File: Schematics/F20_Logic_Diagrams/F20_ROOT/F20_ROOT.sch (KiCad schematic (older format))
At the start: 0 parts

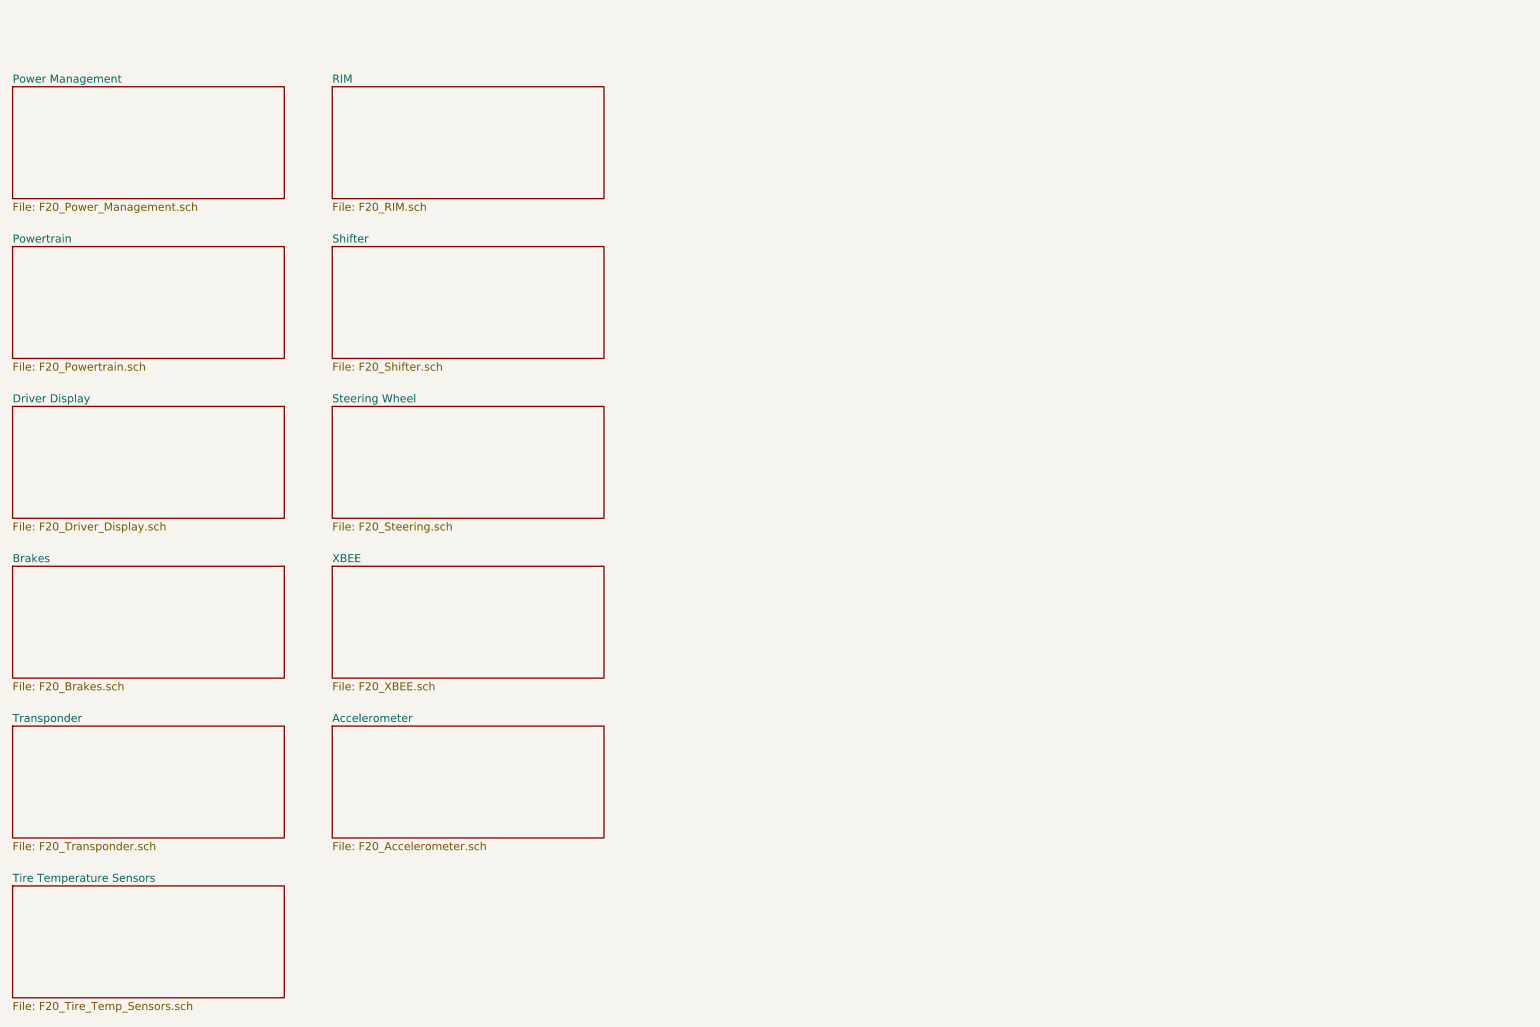
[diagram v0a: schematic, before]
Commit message: Added PDM Layout guide, updated Powertrain wiring, added a Master Connector Pinout guide, added TOC to LogicDiagrams pdf and rearranged them a bit.
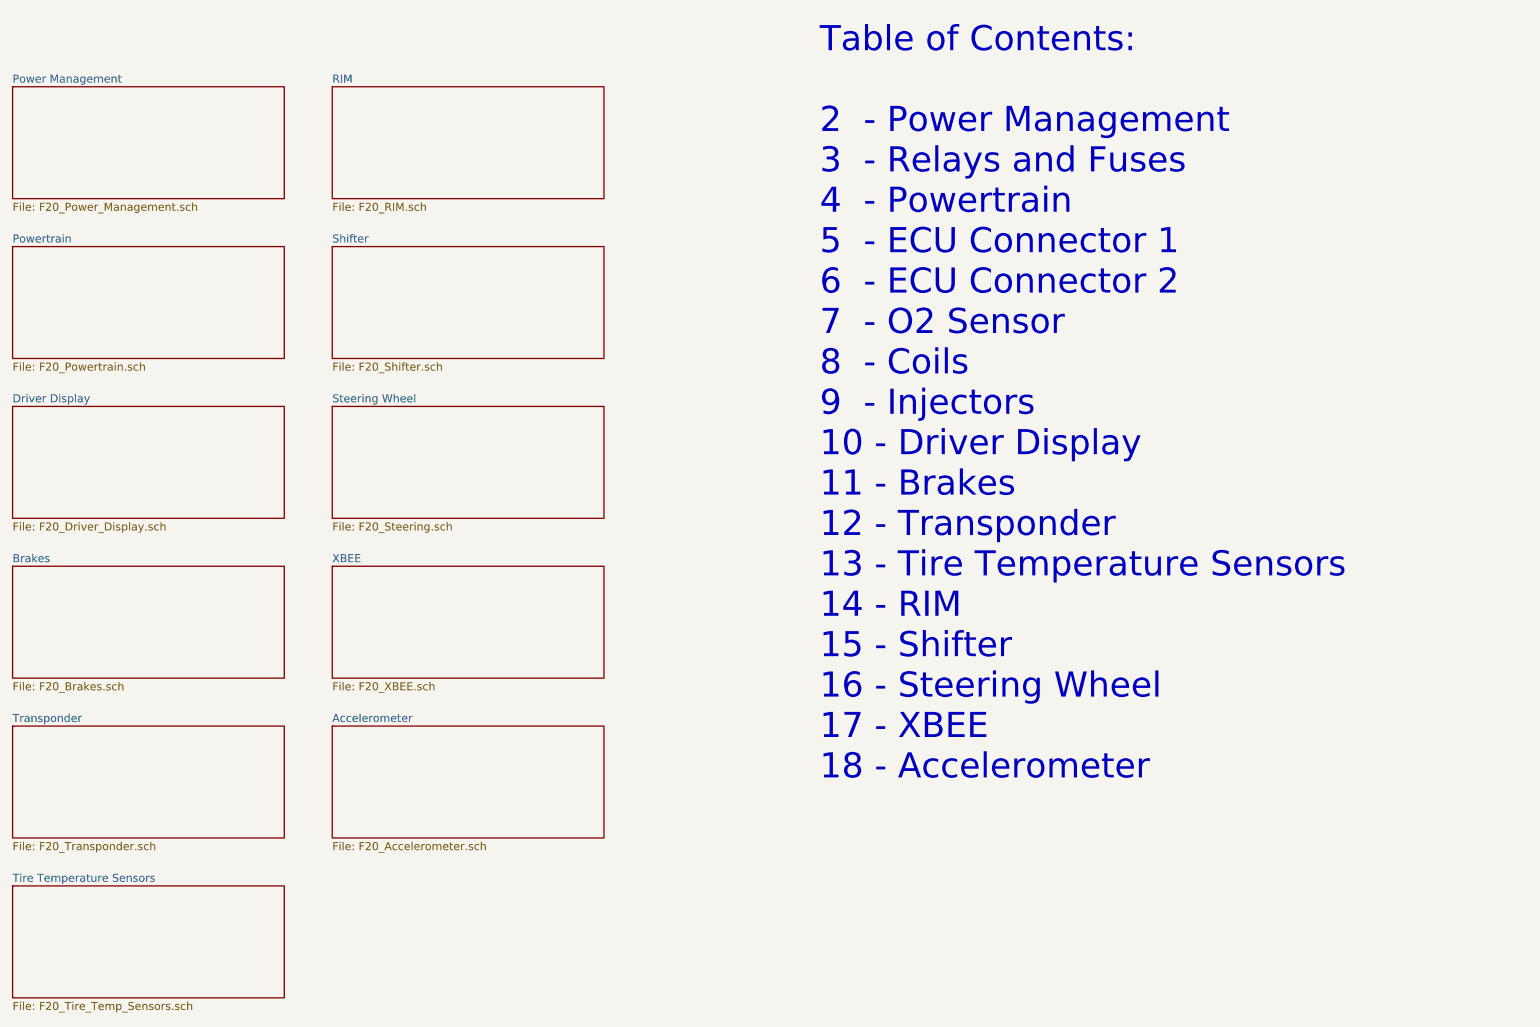
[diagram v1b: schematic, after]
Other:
- note added: "Table of Contents:\n\n2 - Power Management\n3 - Relays and Fuses\n4 - Powertrain\n5 - ECU Connector 1\n6 - ECU Connector 2\n7 - O2 Sensor\n8 - Coils\n9 - Injectors\n10 - Driver Display\n11 - Brakes\n12 - Transponder\n13 - Tire Temperature Sensors\n14 - RIM\n15 - Shifter\n16 - Steering Wheel\n17 - XBEE\n18 - Accelerometer"
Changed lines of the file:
@@
 $EndDescr
+$Sheet
+S 1000 1000 1700 700
+U 5E1D1A8A
+F0 "Power Management" 50
+F1 "F20_Power_Management.sch" 50
+$EndSheet
 $Sheet
 S 1000 2000 1700 700
@@
 F0 "Brakes" 50
 F1 "F20_Brakes.sch" 50
-$EndSheet
-$Sheet
-S 1000 1000 1700 700
-U 5E1D1A8A
-F0 "Power Management" 50
-F1 "F20_Power_Management.sch" 50
 $EndSheet
 $Sheet
@@
 F1 "F20_Accelerometer.sch" 50
 $EndSheet
+Text Notes 6050 5350 0    157  ~ 0
+Table of Contents:\n\n2  - Power Management\n3  - Relays and Fuses\n4  - Powertrain\n5  - ECU Connector 1\n6  - ECU Connector 2\n7  - O2 Sensor\n8  - Coils\n9  - Injectors\n10 - Driver Display\n11 - Brakes\n12 - Transponder\n13 - Tire Temperature Sensors\n14 - RIM\n15 - Shifter\n16 - Steering Wheel\n17 - XBEE\n18 - Accelerometer
 $EndSCHEMATC
